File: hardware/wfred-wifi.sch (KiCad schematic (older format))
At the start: 11 parts, among them K401 UART_ESP, K402 UART_AVR, P401 ESP_BOOTLOAD, U401 ESP-12E

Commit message: Added Reichelt/Mouser part numbers for all parts except ESP12-E/F
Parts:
- C401: Reichelt (none) -> X7R-G0805 100N
- C402: Reichelt (none) -> X5R-G0805 22/25
- K401, K402, P401: Reichelt (none) -> RND 205-00631
- R401, R402: Mouser (none) -> 603-RC0805JR-07100KL
- R403, R404, R405: Mouser (none) -> 603-RC0805JR-0710KL
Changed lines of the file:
@@
 F 2 "Capacitors_SMD:C_0805_HandSoldering" V 2430 2050 30  0001 C CNN
 F 3 "" H 2500 2050 30  0000 C CNN
+F 4 "603-RC0805JR-07100KL" V 2500 2050 60  0001 C CNN "Mouser"
 	1    2500 2050
 	1    0    0    -1
@@
 F 2 "Capacitors_SMD:C_0805_HandSoldering" V 2430 2750 30  0001 C CNN
 F 3 "" H 2500 2750 30  0000 C CNN
+F 4 "603-RC0805JR-07100KL" V 2500 2750 60  0001 C CNN "Mouser"
 	1    2500 2750
 	1    0    0    -1
@@
 F 2 "Pin_Headers:Pin_Header_Straight_1x03_Pitch2.54mm" H 7100 2400 60  0001 C CNN
 F 3 "" H 7100 2400 60  0001 C CNN
+F 4 "RND 205-00631" V 7100 2400 60  0001 C CNN "Reichelt"
 	1    7100 2400
 	1    0    0    -1
@@
 F 2 "Pin_Headers:Pin_Header_Straight_1x02_Pitch2.54mm" H 7100 2800 60  0001 C CNN
 F 3 "" H 7100 2800 60  0001 C CNN
+F 4 "RND 205-00631" V 7100 2800 60  0001 C CNN "Reichelt"
 	1    7100 2800
 	1    0    0    -1
@@
 F 2 "Capacitors_SMD:C_0805_HandSoldering" V 6030 1950 30  0001 C CNN
 F 3 "" H 6100 1950 30  0000 C CNN
+F 4 "603-RC0805JR-0710KL" V 6100 1950 60  0001 C CNN "Mouser"
 	1    6100 1950
 	-1   0    0    1
@@
 F 2 "Capacitors_SMD:C_0805_HandSoldering" V 6030 3350 30  0001 C CNN
 F 3 "" H 6100 3350 30  0000 C CNN
+F 4 "603-RC0805JR-0710KL" V 6100 3350 60  0001 C CNN "Mouser"
 	1    6100 3350
 	-1   0    0    1
@@
 F 2 "Capacitors_SMD:C_0805_HandSoldering" V 6230 1950 30  0001 C CNN
 F 3 "" H 6300 1950 30  0000 C CNN
+F 4 "603-RC0805JR-0710KL" V 6300 1950 60  0001 C CNN "Mouser"
 	1    6300 1950
 	-1   0    0    1
@@
 F 2 "Pin_Headers:Pin_Header_Straight_1x03_Pitch2.54mm" H 7350 2300 60  0001 C CNN
 F 3 "" H 7350 2300 60  0001 C CNN
+F 4 "RND 205-00631" V 7350 2300 60  0001 C CNN "Reichelt"
 	1    7350 2300
 	-1   0    0    -1
@@
 F 2 "Capacitors_SMD:C_0805_HandSoldering" H 1438 2250 30  0001 C CNN
 F 3 "" H 1400 2400 60  0000 C CNN
+F 4 "X7R-G0805 100N" H 1400 2400 60  0001 C CNN "Reichelt"
 	1    1400 2400
 	1    0    0    -1
@@
 F 2 "Capacitors_SMD:C_0805_HandSoldering" H 1738 2250 30  0001 C CNN
 F 3 "" H 1700 2400 60  0000 C CNN
+F 4 "X5R-G0805 22/25" H 1700 2400 60  0001 C CNN "Reichelt"
 	1    1700 2400
 	1    0    0    -1

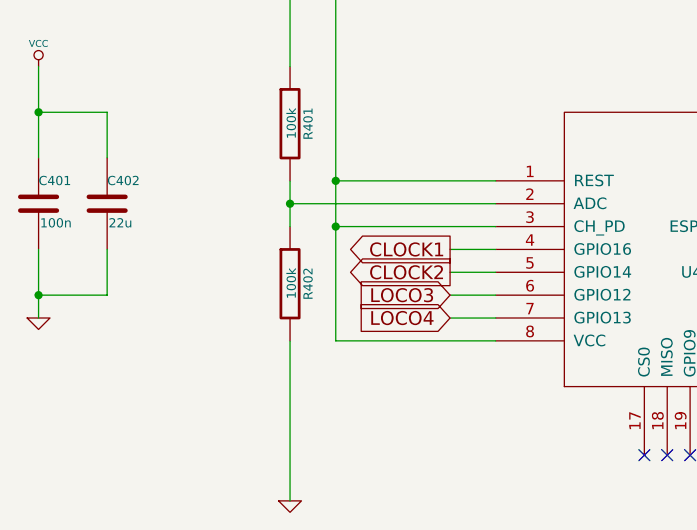
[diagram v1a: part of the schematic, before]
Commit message: Changed low battery detection after first test run
- changed hardware: Reduced R402 from 100kOhm to 47kOhm so battery
  voltage can be measured above 2V
- changed firmware accordingly (instead of * 2 now calculate * 147 / 47
  and * 1000 / 1024 to correct for 10Bit = 1V
- raised thresholds for low and empty battery voltate - on first test,
  battery still showed 1988mV one minute and system was down the next
  minute (after 12 hours)
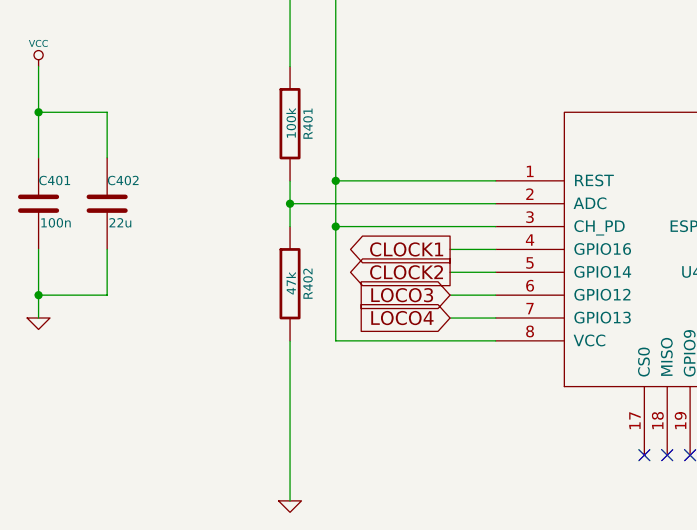
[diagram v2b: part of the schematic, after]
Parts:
- R402: value 100k -> 47k
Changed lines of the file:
@@
 P 2500 2750
 F 0 "R402" V 2580 2750 40  0000 C CNN
-F 1 "100k" V 2507 2751 40  0000 C CNN
+F 1 "47k" V 2507 2751 40  0000 C CNN
 F 2 "Capacitors_SMD:C_0805_HandSoldering" V 2430 2750 30  0001 C CNN
 F 3 "" H 2500 2750 30  0000 C CNN

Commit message: Created new 3D renderings
- In the process, kicad "rescued" some symbols
- Also added the value to the crystal in the schematic
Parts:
- C401, C402: symbol C -> C-RESCUE-wfred_rev2
- R401, R402, R403, R404, R405: symbol R -> R-RESCUE-wfred_rev2
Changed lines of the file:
@@
 EESchema Schematic File Version 2
+LIBS:wfred_rev2-rescue
 LIBS:power
 LIBS:device
@@
 LIBS:my_devices
 LIBS:ESP8266
-LIBS:wfred_loconet_clock-cache
+LIBS:wfred_rev2-cache
 EELAYER 25 0
 EELAYER END
 $Descr A4 11693 8268
 encoding utf-8
-Sheet 4 5
+Sheet 4 4
 Title "Wireless FREDI (and clock interface)"
 Date "2017-11-19"
@@
 	2500 1500 2500 1800
 $Comp
-L R R401
+L R-RESCUE-wfred_rev2 R401
 U 1 1 5A11AE00
 P 2500 2050
@@
 $EndComp
 $Comp
-L R R402
+L R-RESCUE-wfred_rev2 R402
 U 1 1 5A11AE49
 P 2500 2750
@@
 Connection ~ 2500 2400
 $Comp
-L GND #PWR037
+L GND-RESCUE-wfred_rev2 #PWR037
 U 1 1 5A11B098
 P 2500 3700
@@
 Connection ~ 2700 2500
 $Comp
-L GND #PWR039
+L GND-RESCUE-wfred_rev2 #PWR039
 U 1 1 5A11E30D
 P 6700 3700
@@
 	5200 2700 6750 2700
 $Comp
-L GND #PWR041
+L GND-RESCUE-wfred_rev2 #PWR041
 U 1 1 5A11FC27
 P 7850 2500
@@
 $EndComp
 $Comp
-L R R403
+L R-RESCUE-wfred_rev2 R403
 U 1 1 5A11FF91
 P 6100 1950
@@
 $EndComp
 $Comp
-L R R404
+L R-RESCUE-wfred_rev2 R404
 U 1 1 5A11FFE4
 P 6100 3350
@@
 $EndComp
 $Comp
-L R R405
+L R-RESCUE-wfred_rev2 R405
 U 1 1 5A120047
 P 6300 1950
@@
 	6100 2900 6100 3100
 $Comp
-L GND #PWR042
+L GND-RESCUE-wfred_rev2 #PWR042
 U 1 1 5A120E87
 P 6100 3700
@@
 	5400 2600 5200 2600
 $Comp
-L C C401
+L C-RESCUE-wfred_rev2 C401
 U 1 1 5A127BCA
 P 1400 2400
+AR Path="/5A127BCA" Ref="C401"  Part="1"
+AR Path="/5A122619/5A127BCA" Ref="C401"  Part="1"
 F 0 "C401" H 1400 2500 40  0000 L CNN
 F 1 "100n" H 1406 2315 40  0000 L CNN
@@
 	1400 1800 1400 2200
 $Comp
-L GND #PWR044
+L GND-RESCUE-wfred_rev2 #PWR044
 U 1 1 5A127CDB
 P 1400 2900
@@
 	1400 2900 1400 2600
 $Comp
-L C C402
+L C-RESCUE-wfred_rev2 C402
 U 1 1 5A199174
 P 1700 2400
+AR Path="/5A199174" Ref="C402"  Part="1"
+AR Path="/5A122619/5A199174" Ref="C402"  Part="1"
 F 0 "C402" H 1700 2500 40  0000 L CNN
 F 1 "22u" H 1706 2315 40  0000 L CNN

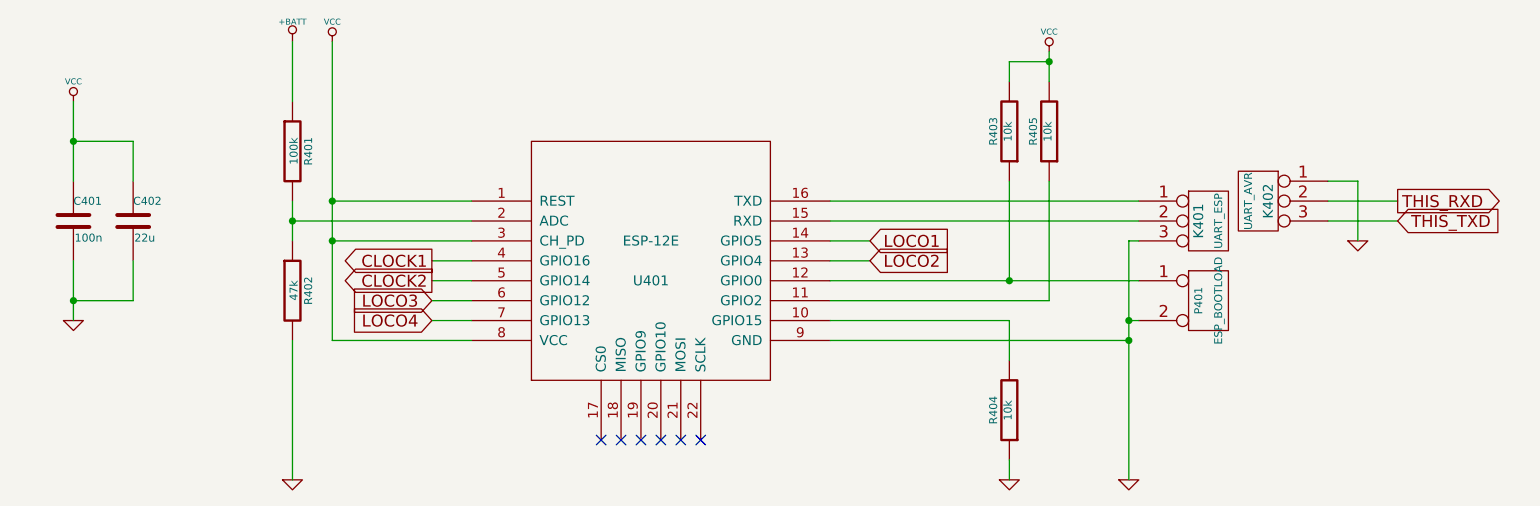
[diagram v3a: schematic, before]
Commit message: Switched schematic over to LiPo cell
- Removed AA battery holder
- Removed switching power regulator
- Added micro USB connector
- Added two pin battery connector
- Added LiPo charging IC
- Added 3.0V linear regulator
- Replaced ATMega328 with ATMega32
- Added F5-F8 keys
- Removed SHIFT2 key
- Moved LOCO keys from ESP to ATMega32
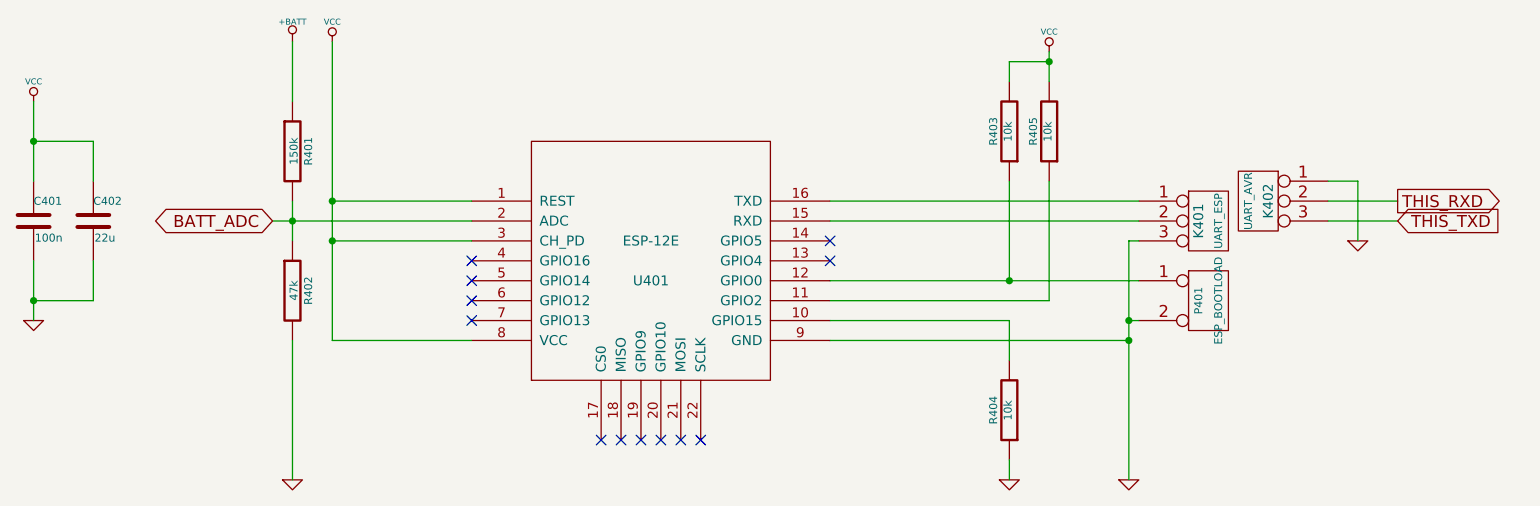
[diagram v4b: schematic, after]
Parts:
- R401: value 100k -> 150k
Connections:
- net BATT_ADC: now reaches R401.2, R402.1, U401.2 (ADC)
- net CLOCK1: no longer names the net of U401.4 (GPIO16)
- net CLOCK2: no longer names the net of U401.5 (GPIO14)
- net LOCO1: no longer names the net of U401.14 (GPIO5)
- net LOCO2: no longer names the net of U401.13 (GPIO4)
- net LOCO3: no longer names the net of U401.6 (GPIO12)
- net LOCO4: no longer names the net of U401.7 (GPIO13)
- no-connect marks 6 -> 12
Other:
- moved on the sheet: C401, C402
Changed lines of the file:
@@
 LIBS:my_devices
 LIBS:ESP8266
+LIBS:LDL1117S30R
+LIBS:MCP73831T-2ACI_OT
 LIBS:wfred_rev2-cache
 EELAYER 25 0
@@
 $EndComp
 $Comp
-L +BATT #PWR036
+L +BATT #PWR041
 U 1 1 5A11AB98
 P 2500 1500
-F 0 "#PWR036" H 2500 1450 20  0001 C CNN
+F 0 "#PWR041" H 2500 1450 20  0001 C CNN
 F 1 "+BATT" H 2500 1600 30  0000 C CNN
 F 2 "" H 2500 1500 60  0001 C CNN
@@
 P 2500 2050
 F 0 "R401" V 2580 2050 40  0000 C CNN
-F 1 "100k" V 2507 2051 40  0000 C CNN
+F 1 "150k" V 2507 2051 40  0000 C CNN
 F 2 "Capacitors_SMD:C_0805_HandSoldering" V 2430 2050 30  0001 C CNN
 F 3 "" H 2500 2050 30  0000 C CNN
@@
 	2500 2300 2500 2500
 Wire Wire Line
-	3400 2400 2500 2400
+	2400 2400 3400 2400
 Connection ~ 2500 2400
 $Comp
-L GND-RESCUE-wfred_rev2 #PWR037
+L GND-RESCUE-wfred_rev2 #PWR042
 U 1 1 5A11B098
 P 2500 3700
-F 0 "#PWR037" H 2500 3700 30  0001 C CNN
+F 0 "#PWR042" H 2500 3700 30  0001 C CNN
 F 1 "GND" H 2500 3630 30  0001 C CNN
 F 2 "" H 2500 3700 60  0001 C CNN
@@
 NoConn ~ 4550 3500
 $Comp
-L VCC #PWR038
+L VCC #PWR043
 U 1 1 5A11E004
 P 2700 1500
-F 0 "#PWR038" H 2700 1600 30  0001 C CNN
+F 0 "#PWR043" H 2700 1600 30  0001 C CNN
 F 1 "VCC" H 2700 1600 30  0000 C CNN
 F 2 "" H 2700 1500 60  0001 C CNN
@@
 Connection ~ 2700 2500
 $Comp
-L GND-RESCUE-wfred_rev2 #PWR039
+L GND-RESCUE-wfred_rev2 #PWR044
 U 1 1 5A11E30D
 P 6700 3700
-F 0 "#PWR039" H 6700 3700 30  0001 C CNN
+F 0 "#PWR044" H 6700 3700 30  0001 C CNN
 F 1 "GND" H 6700 3630 30  0001 C CNN
 F 2 "" H 6700 3700 60  0001 C CNN
@@
 Connection ~ 6700 3000
 $Comp
-L VCC #PWR040
+L VCC #PWR045
 U 1 1 5A11E4AA
 P 6300 1550
-F 0 "#PWR040" H 6300 1650 30  0001 C CNN
+F 0 "#PWR045" H 6300 1650 30  0001 C CNN
 F 1 "VCC" H 6300 1650 30  0000 C CNN
 F 2 "" H 6300 1550 60  0001 C CNN
@@
 	5200 2700 6750 2700
 $Comp
-L GND-RESCUE-wfred_rev2 #PWR041
+L GND-RESCUE-wfred_rev2 #PWR046
 U 1 1 5A11FC27
 P 7850 2500
-F 0 "#PWR041" H 7850 2500 30  0001 C CNN
+F 0 "#PWR046" H 7850 2500 30  0001 C CNN
 F 1 "GND" H 7850 2430 30  0001 C CNN
 F 2 "" H 7850 2500 60  0001 C CNN
@@
 	6100 2900 6100 3100
 $Comp
-L GND-RESCUE-wfred_rev2 #PWR042
+L GND-RESCUE-wfred_rev2 #PWR047
 U 1 1 5A120E87
 P 6100 3700
-F 0 "#PWR042" H 6100 3700 30  0001 C CNN
+F 0 "#PWR047" H 6100 3700 30  0001 C CNN
 F 1 "GND" H 6100 3630 30  0001 C CNN
 F 2 "" H 6100 3700 60  0001 C CNN
@@
 	6750 2900 6700 2900
 Connection ~ 6700 2900
-Text GLabel 5400 2500 2    60   Input ~ 0
-LOCO1
-Text GLabel 5400 2600 2    60   Input ~ 0
-LOCO2
-Text GLabel 3200 2800 0    60   Input ~ 0
-LOCO3
-Text GLabel 3200 2900 0    60   Input ~ 0
-LOCO4
-Text GLabel 3200 2600 0    60   Output ~ 0
-CLOCK1
-Text GLabel 3200 2700 0    60   Output ~ 0
-CLOCK2
-Wire Wire Line
-	3200 2600 3400 2600
-Wire Wire Line
-	3400 2700 3200 2700
-Wire Wire Line
-	3400 2800 3200 2800
-Wire Wire Line
-	3200 2900 3400 2900
-Wire Wire Line
-	5200 2500 5400 2500
-Wire Wire Line
-	5400 2600 5200 2600
 $Comp
 L C-RESCUE-wfred_rev2 C401
 U 1 1 5A127BCA
-P 1400 2400
+P 1200 2400
 AR Path="/5A127BCA" Ref="C401"  Part="1"
 AR Path="/5A122619/5A127BCA" Ref="C401"  Part="1"
-F 0 "C401" H 1400 2500 40  0000 L CNN
-F 1 "100n" H 1406 2315 40  0000 L CNN
-F 2 "Capacitors_SMD:C_0805_HandSoldering" H 1438 2250 30  0001 C CNN
-F 3 "" H 1400 2400 60  0000 C CNN
-F 4 "X7R-G0805 100N" H 1400 2400 60  0001 C CNN "Reichelt"
-	1    1400 2400
-	1    0    0    -1
-$EndComp
-$Comp
-L VCC #PWR043
+F 0 "C401" H 1200 2500 40  0000 L CNN
+F 1 "100n" H 1206 2315 40  0000 L CNN
+F 2 "Capacitors_SMD:C_0805_HandSoldering" H 1238 2250 30  0001 C CNN
+F 3 "" H 1200 2400 60  0000 C CNN
+F 4 "X7R-G0805 100N" H 1200 2400 60  0001 C CNN "Reichelt"
+	1    1200 2400
+	1    0    0    -1
+$EndComp
+$Comp
+L VCC #PWR048
 U 1 1 5A127C0E
-P 1400 1800
-F 0 "#PWR043" H 1400 1900 30  0001 C CNN
-F 1 "VCC" H 1400 1900 30  0000 C CNN
-F 2 "" H 1400 1800 60  0001 C CNN
-F 3 "" H 1400 1800 60  0001 C CNN
-	1    1400 1800
-	1    0    0    -1
-$EndComp
-Wire Wire Line
-	1400 1800 1400 2200
-$Comp
-L GND-RESCUE-wfred_rev2 #PWR044
+P 1200 1800
+F 0 "#PWR048" H 1200 1900 30  0001 C CNN
+F 1 "VCC" H 1200 1900 30  0000 C CNN
+F 2 "" H 1200 1800 60  0001 C CNN
+F 3 "" H 1200 1800 60  0001 C CNN
+	1    1200 1800
+	1    0    0    -1
+$EndComp
+Wire Wire Line
+	1200 1800 1200 2200
+$Comp
+L GND-RESCUE-wfred_rev2 #PWR049
 U 1 1 5A127CDB
-P 1400 2900
-F 0 "#PWR044" H 1400 2900 30  0001 C CNN
-F 1 "GND" H 1400 2830 30  0001 C CNN
-F 2 "" H 1400 2900 60  0001 C CNN
-F 3 "" H 1400 2900 60  0001 C CNN
-	1    1400 2900
-	1    0    0    -1
-$EndComp
-Wire Wire Line
-	1400 2900 1400 2600
+P 1200 2900
+F 0 "#PWR049" H 1200 2900 30  0001 C CNN
+F 1 "GND" H 1200 2830 30  0001 C CNN
+F 2 "" H 1200 2900 60  0001 C CNN
+F 3 "" H 1200 2900 60  0001 C CNN
+	1    1200 2900
+	1    0    0    -1
+$EndComp
+Wire Wire Line
+	1200 2900 1200 2600
 $Comp
 L C-RESCUE-wfred_rev2 C402
 U 1 1 5A199174
-P 1700 2400
+P 1500 2400
 AR Path="/5A199174" Ref="C402"  Part="1"
 AR Path="/5A122619/5A199174" Ref="C402"  Part="1"
-F 0 "C402" H 1700 2500 40  0000 L CNN
-F 1 "22u" H 1706 2315 40  0000 L CNN
-F 2 "Capacitors_SMD:C_0805_HandSoldering" H 1738 2250 30  0001 C CNN
-F 3 "" H 1700 2400 60  0000 C CNN
-F 4 "X5R-G0805 22/25" H 1700 2400 60  0001 C CNN "Reichelt"
-	1    1700 2400
-	1    0    0    -1
-$EndComp
-Wire Wire Line
-	1400 2000 1700 2000
-Wire Wire Line
-	1700 2000 1700 2200
-Connection ~ 1400 2000
-Wire Wire Line
-	1700 2600 1700 2800
-Wire Wire Line
-	1700 2800 1400 2800
-Connection ~ 1400 2800
+F 0 "C402" H 1500 2500 40  0000 L CNN
+F 1 "22u" H 1506 2315 40  0000 L CNN
+F 2 "Capacitors_SMD:C_0805_HandSoldering" H 1538 2250 30  0001 C CNN
+F 3 "" H 1500 2400 60  0000 C CNN
+F 4 "X5R-G0805 22/25" H 1500 2400 60  0001 C CNN "Reichelt"
+	1    1500 2400
+	1    0    0    -1
+$EndComp
+Wire Wire Line
+	1200 2000 1500 2000
+Wire Wire Line
+	1500 2000 1500 2200
+Connection ~ 1200 2000
+Wire Wire Line
+	1500 2600 1500 2800
+Wire Wire Line
+	1500 2800 1200 2800
+Connection ~ 1200 2800
+Text GLabel 2400 2400 0    60   BiDi ~ 0
+BATT_ADC
+NoConn ~ 5200 2500
+NoConn ~ 5200 2600
+NoConn ~ 3400 2600
+NoConn ~ 3400 2700
+NoConn ~ 3400 2800
+NoConn ~ 3400 2900
 $EndSCHEMATC

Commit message: Added ESP reset connection to AVR
- Enables ESP to go into deep sleep and be woken up by AVR
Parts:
- added R406: 10k, Capacitors_SMD:C_0805_HandSoldering, symbol R-RESCUE-wfred_rev2
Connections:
- net VCC: now also R406.2; no longer U401.1 (REST)
- new net ESP_RESET: R406.1, U401.1 (REST)
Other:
- moved on the sheet: R401
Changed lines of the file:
@@
 $EndComp
 Wire Wire Line
-	2500 1500 2500 1800
+	2500 1500 2500 1700
 $Comp
 L R-RESCUE-wfred_rev2 R401
 U 1 1 5A11AE00
-P 2500 2050
-F 0 "R401" V 2580 2050 40  0000 C CNN
-F 1 "150k" V 2507 2051 40  0000 C CNN
-F 2 "Capacitors_SMD:C_0805_HandSoldering" V 2430 2050 30  0001 C CNN
-F 3 "" H 2500 2050 30  0000 C CNN
-F 4 "603-RC0805JR-07100KL" V 2500 2050 60  0001 C CNN "Mouser"
-	1    2500 2050
+P 2500 1950
+F 0 "R401" V 2580 1950 40  0000 C CNN
+F 1 "150k" V 2507 1951 40  0000 C CNN
+F 2 "Capacitors_SMD:C_0805_HandSoldering" V 2430 1950 30  0001 C CNN
+F 3 "" H 2500 1950 30  0000 C CNN
+F 4 "603-RC0805JR-07100KL" V 2500 1950 60  0001 C CNN "Mouser"
+	1    2500 1950
 	1    0    0    -1
 $EndComp
@@
 $EndComp
 Wire Wire Line
-	2500 2300 2500 2500
+	2500 2200 2500 2500
 Wire Wire Line
 	2400 2400 3400 2400
@@
 	2700 1500 2700 3000
 Wire Wire Line
-	2700 2300 3400 2300
-Wire Wire Line
 	2700 3000 3400 3000
-Connection ~ 2700 2300
 Wire Wire Line
 	3400 2500 2700 2500
@@
 $EndComp
 Wire Wire Line
-	1200 2900 1200 2600
+	1200 2600 1200 2900
 $Comp
 L C-RESCUE-wfred_rev2 C402
@@
 NoConn ~ 3400 2800
 NoConn ~ 3400 2900
+$Comp
+L R-RESCUE-wfred_rev2 R406
+U 1 1 5BDF6A62
+P 3200 1950
+F 0 "R406" V 3280 1950 40  0000 C CNN
+F 1 "10k" V 3207 1951 40  0000 C CNN
+F 2 "Capacitors_SMD:C_0805_HandSoldering" V 3130 1950 30  0001 C CNN
+F 3 "" H 3200 1950 30  0000 C CNN
+F 4 "603-RC0805JR-0710KL" V 3200 1950 60  0001 C CNN "Mouser"
+	1    3200 1950
+	-1   0    0    1
+$EndComp
+Wire Wire Line
+	3200 2200 3200 2300
+Wire Wire Line
+	2400 2300 3400 2300
+$Comp
+L VCC #PWR050
+U 1 1 5BDF6B6E
+P 3200 1500
+F 0 "#PWR050" H 3200 1600 30  0001 C CNN
+F 1 "VCC" H 3200 1600 30  0000 C CNN
+F 2 "" H 3200 1500 60  0001 C CNN
+F 3 "" H 3200 1500 60  0001 C CNN
+	1    3200 1500
+	1    0    0    -1
+$EndComp
+Wire Wire Line
+	3200 1500 3200 1700
+Text GLabel 2400 2300 0    60   Input ~ 0
+ESP_RESET
+Connection ~ 3200 2300
 $EndSCHEMATC
